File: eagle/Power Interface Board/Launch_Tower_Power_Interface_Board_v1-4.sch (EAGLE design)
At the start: 35 parts

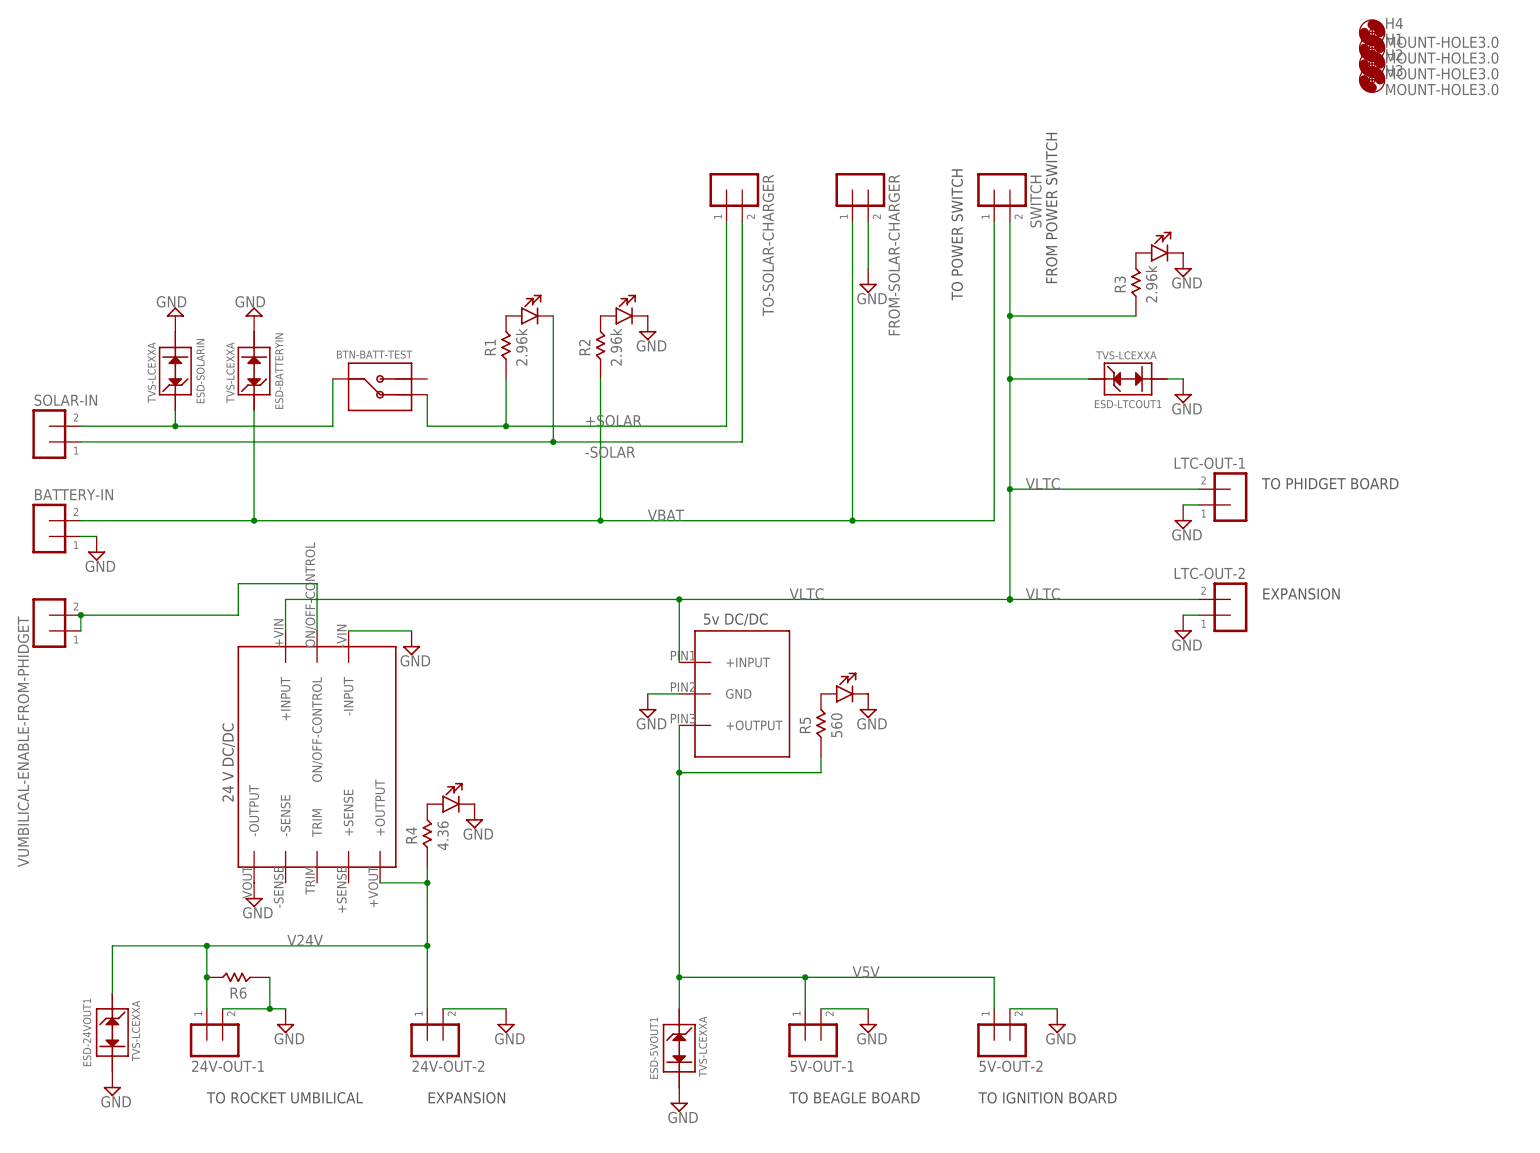
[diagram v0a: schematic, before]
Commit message: Clean up of power distribution board, lots of small changes, including rcl_custom 0805 packages, ERC and DRC issues, cleaned up tnames, etc.
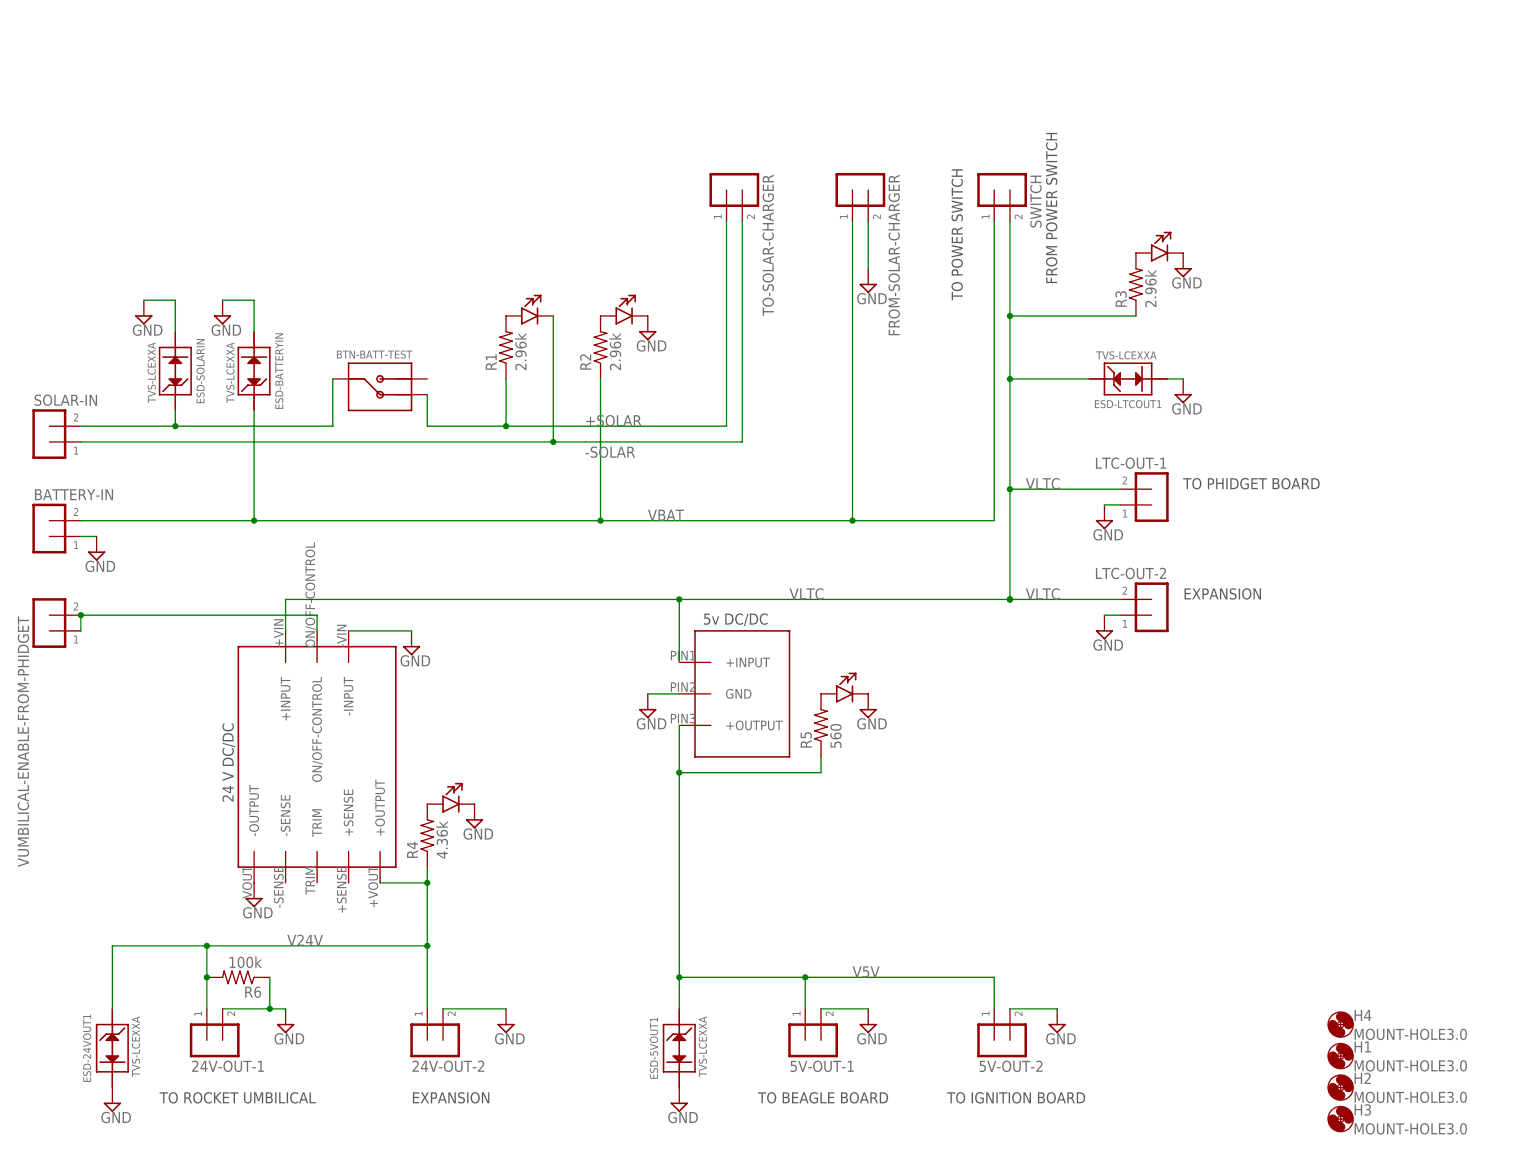
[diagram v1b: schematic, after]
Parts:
- R1, R2, R3, R5: device launch-tower:RESISTOR-0805 -> rcl_custom:R-US_0805-B
- R4: value 4.36 -> 4.36k; device launch-tower:RESISTOR-0805 -> rcl_custom:R-US_0805-B
- R6: value (none) -> 100k; device launch-tower:RESISTOR-0805 -> rcl_custom:R-US_0805-B
- renumbered U$1 to DC2, U$2 to DC1
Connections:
- net +SOLAR: now also R1.1; no longer R1.ANODE
- net GND: now also R6.1; no longer R6.ANODE
- net N$1: now also R1.2; no longer R1.CATHODE
- net N$2: now also R2.2; no longer R2.CATHODE
- net N$3: now also R3.2; no longer R3.CATHODE
- net N$4: now also R5.2; no longer R5.CATHODE
- net N$5: now also R4.2; no longer R4.CATHODE
- net V24V: now also R4.1, R6.2; no longer R4.ANODE, R6.CATHODE
- net V5V: now also R5.1; no longer R5.ANODE
- net VBAT: now also R2.1; no longer R2.ANODE
- net VLTC: now also R3.1; no longer R3.ANODE
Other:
- moved on the sheet: ESD-24VOUT1, H1, H2, H3, H4, LTC-OUT-1, LTC-OUT-2

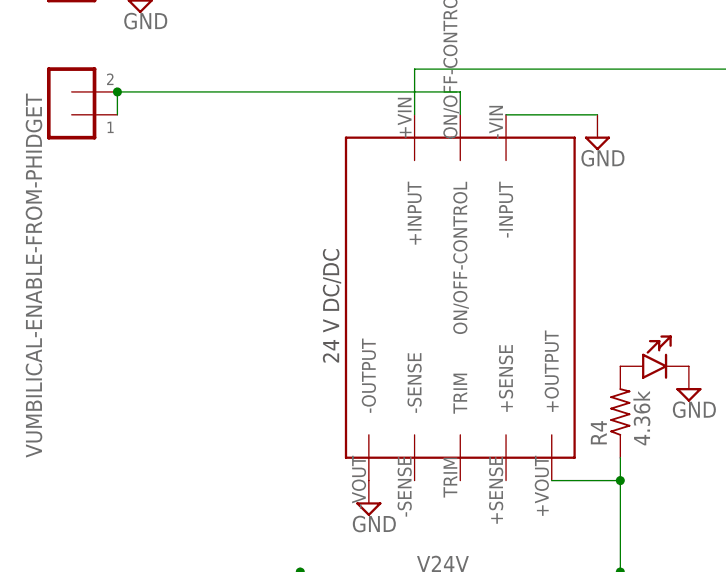
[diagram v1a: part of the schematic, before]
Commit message: Added SPS part number to schematic and board.
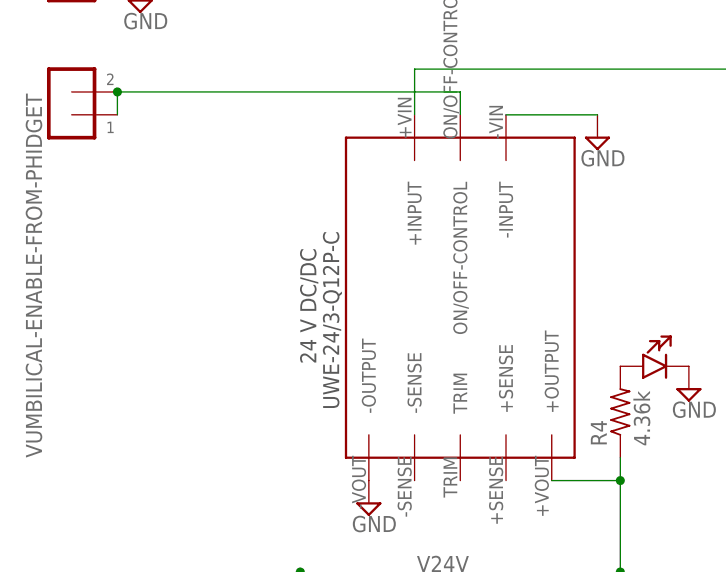
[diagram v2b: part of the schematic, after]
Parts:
- DC2: value DC/DC_CONV_24V -> UWE-24/3-Q12P-C
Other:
- note added: "UWE-24/3-Q12P-C"
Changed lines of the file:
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@@
 <?xml version="1.0" encoding="utf-8"?>
 <!DOCTYPE eagle SYSTEM "eagle.dtd">
-<eagle version="6.2">
+<eagle version="6.4">
 <drawing>
 <settings>
@@
 <part name="SUPPLY5" library="supply2" deviceset="GND" device=""/>
 <part name="SUPPLY13" library="supply2" deviceset="GND" device=""/>
-<part name="DC2" library="launch-tower" deviceset="DC/DC_CONV_24V" device=""/>
+<part name="DC2" library="launch-tower" deviceset="DC/DC_CONV_24V" device="" value="UWE-24/3-Q12P-C"/>
 <part name="SUPPLY15" library="supply2" deviceset="GND" device=""/>
 <part name="SUPPLY16" library="supply2" deviceset="GND" device=""/>
@@
 <text x="127" y="10.16" size="1.778" layer="97">TO BEAGLE BOARD</text>
 <text x="157.48" y="10.16" size="1.778" layer="97">TO IGNITION BOARD</text>
-<text x="42.418" y="58.674" size="1.778" layer="97" rot="R90">24 V DC/DC</text>
+<text x="42.418" y="53.594" size="1.778" layer="97" rot="R90">UWE-24/3-Q12P-C</text>
 <text x="30.48" y="10.16" size="1.778" layer="97">TO ROCKET UMBILICAL</text>
 <text x="71.12" y="10.16" size="1.778" layer="97">EXPANSION</text>
+<text x="39.878" y="58.674" size="1.778" layer="97" rot="R90">24 V DC/DC</text>
 </plain>
 <instances>
